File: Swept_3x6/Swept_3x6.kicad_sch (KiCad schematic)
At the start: 94 parts, among them SW10 SW_Push, SW10_r1 SW_Push, SW11 SW_Push, SW11_r1 SW_Push, SW12 SW_Push, SW12_r1 SW_Push, SW13 SW_Push, SW13_r1 SW_Push, SW14 SW_Push, SW14_r1 SW_Push, SW15 SW_Push, SW15_r1 SW_Push, SW16 SW_Push, SW16_r1 SW_Push, SW17 SW_Push, SW17_r1 SW_Push, SW18 SW_Push, SW18_r1 SW_Push, SW19 SW_Push, SW19_r1 SW_Push, SW2 SW_Push, SW20 SW_Push, SW20_r1 SW_Push, SW21 SW_Push, SW21_r1 SW_Push, SW22 SW_Push, SW22_r1 SW_Push, SW2_r1 SW_Push, SW3 SW_Push, SW3_r1 SW_Push, SW4 SW_Push, SW4_r1 SW_Push, SW5 SW_Push, SW5_r1 SW_Push, SW6 SW_Push, SW6_r1 SW_Push, SW7 SW_Push, SW7_r1 SW_Push, SW8 SW_Push, SW8_r1 SW_Push, SW9 SW_Push, SW9_r1 SW_Push, U1 ProMicro-kbd, U2 ProMicro-kbd

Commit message: Added support for Kailh hot-swap sockets.
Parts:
- D0, D1, D10, D11, D12, D13, D14, D15, D16, D17, D18, D19, D2, D20, D3, D4, D5, D6, D7, D8, D9, Dr0, Dr1, Dr10, Dr11, Dr12, Dr13, Dr14, Dr15, Dr16, Dr17, Dr18, Dr19, Dr2, Dr20, Dr3, Dr4, Dr5, Dr6, Dr7, Dr8, Dr9: LCSC (none) -> C2099
- SW10, SW10_r1, SW11, SW11_r1, SW12, SW12_r1, SW13, SW13_r1, SW14, SW14_r1, SW15, SW15_r1, SW16, SW16_r1, SW17, SW17_r1, SW18, SW18_r1, SW19, SW19_r1, SW2, SW20, SW20_r1, SW21, SW21_r1, SW22, SW22_r1, SW2_r1, SW3, SW3_r1, SW4, SW4_r1, SW5, SW5_r1, SW6, SW6_r1, SW7, SW7_r1, SW8, SW8_r1, SW9, SW9_r1: footprint aym1607:choc-v1-with-millmax -> keyswitches:Kailh_socket_PG1350_optional

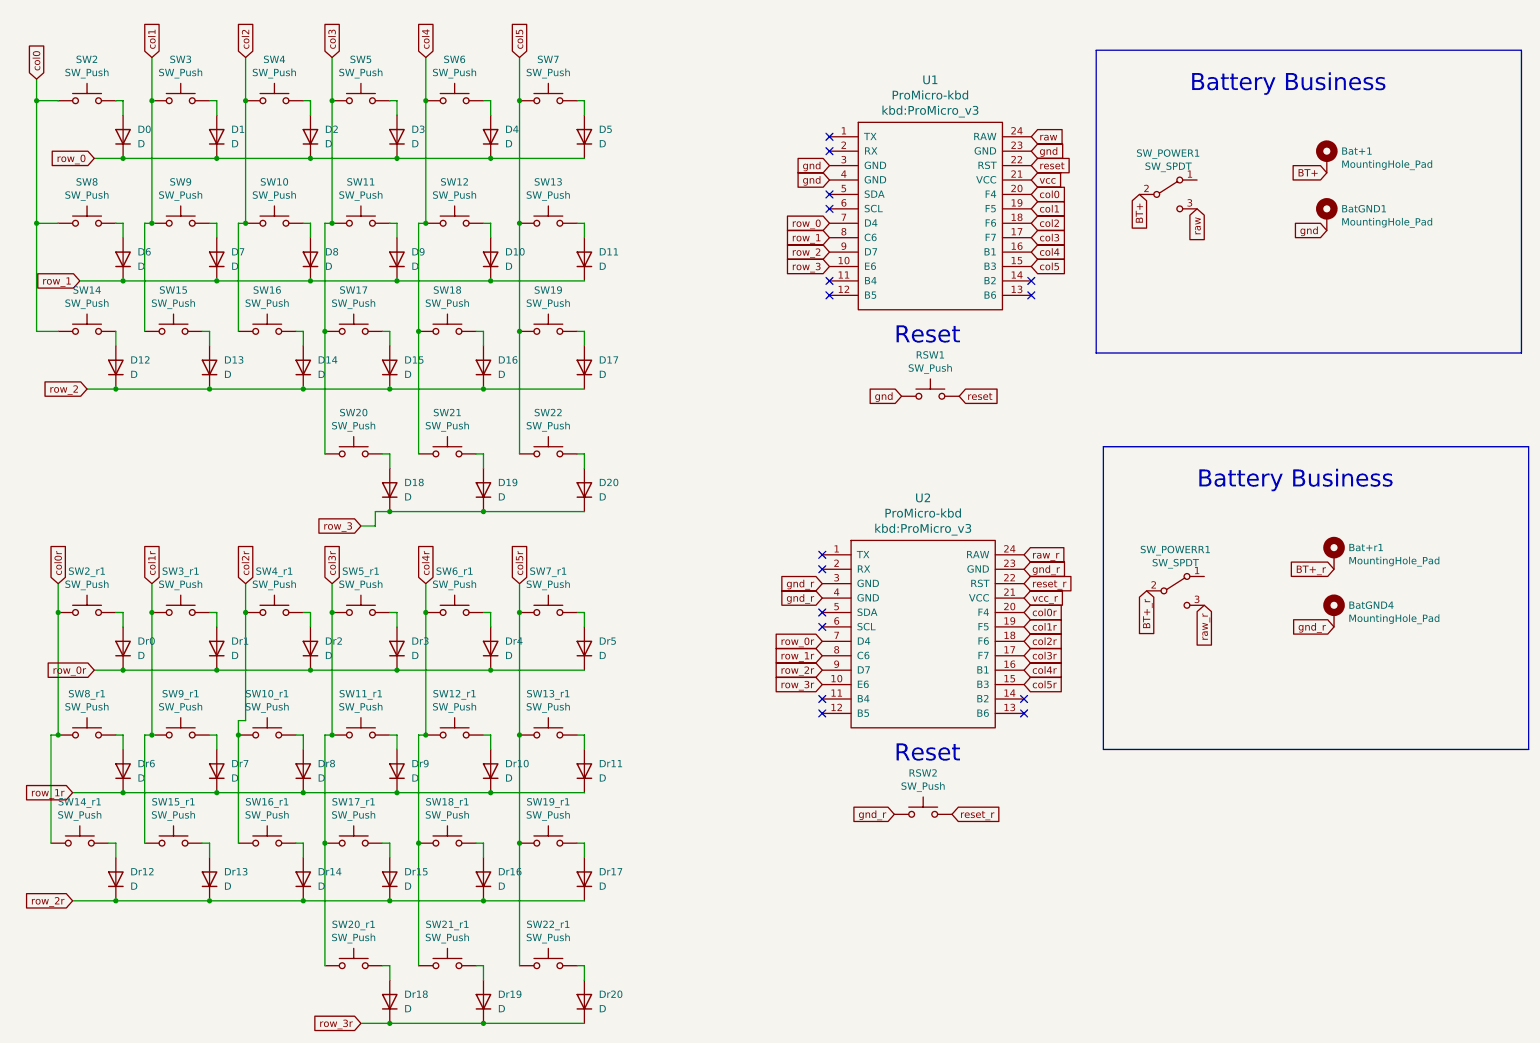
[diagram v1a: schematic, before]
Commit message: Added nice!view suppor for 3x6
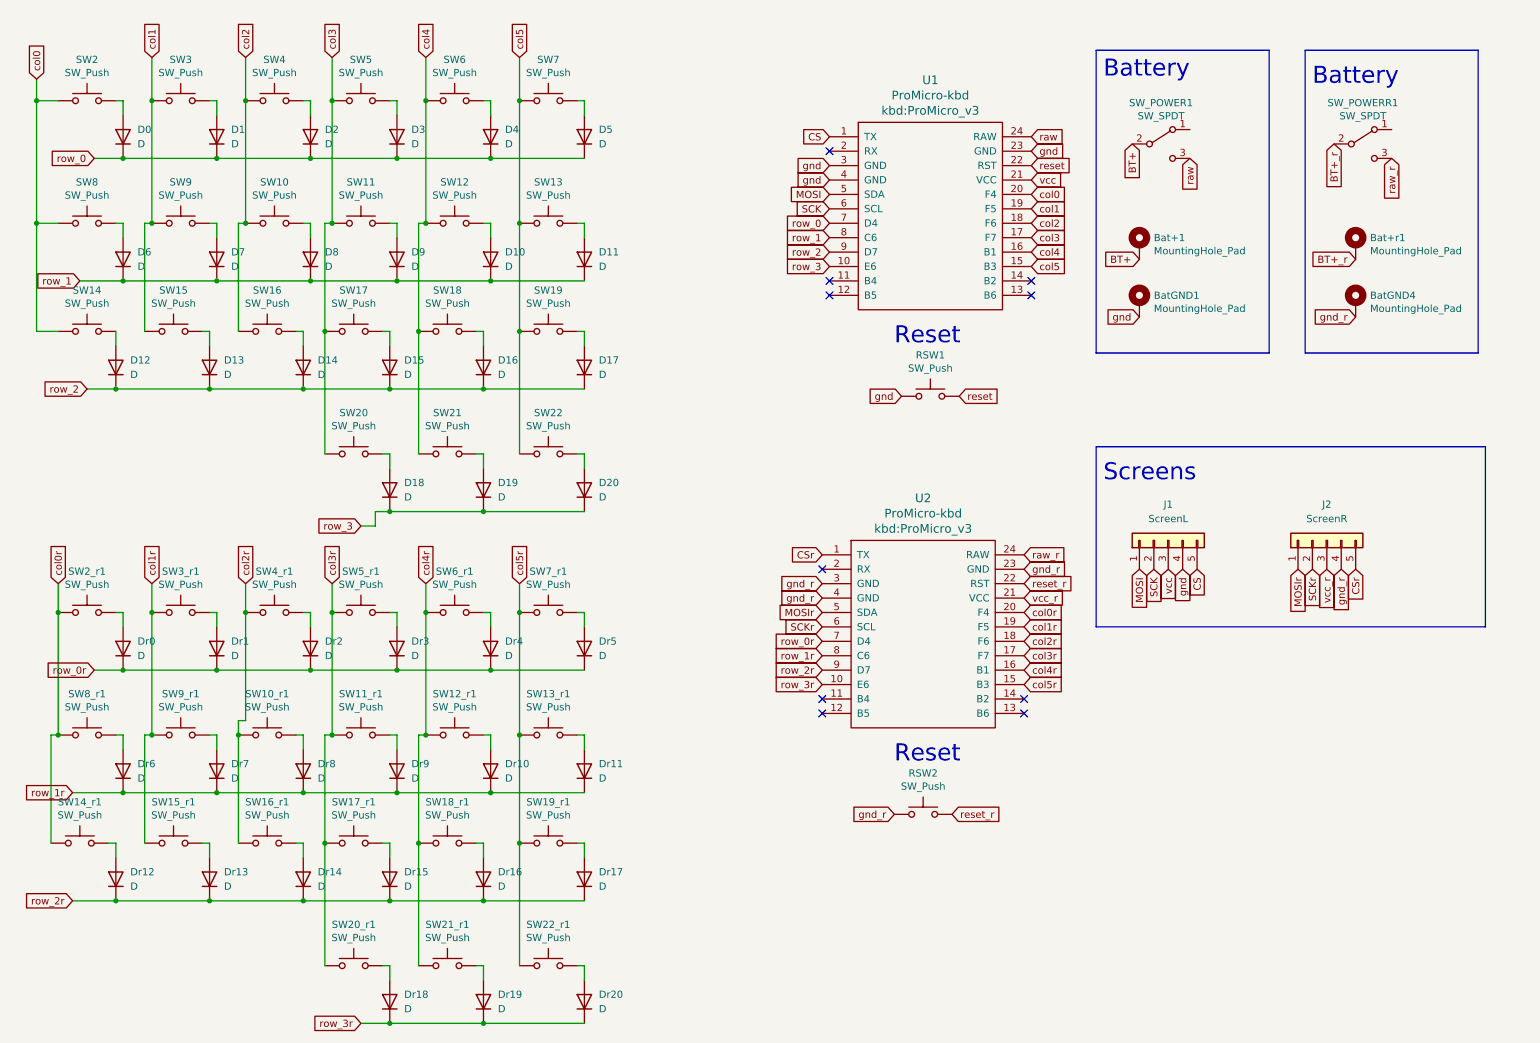
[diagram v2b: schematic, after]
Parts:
- added J1: ScreenL, symbol Connector_Generic:Conn_01x05
- added J2: ScreenR, symbol Connector_Generic:Conn_01x05
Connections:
- net gnd: now also J1.4 (Pin_4)
- net gnd_r: now also J2.4 (Pin_4)
- net vcc: now also J1.3 (Pin_3)
- net vcc_r: now also J2.3 (Pin_3)
- net CS: now reaches U1.1 (TX)
- net CS: now also J1.5 (Pin_5)
- net MOSI: now reaches U1.5 (SDA)
- net MOSI: now also J1.1 (Pin_1)
- net SCK: now reaches U1.6 (SCL)
- net SCK: now also J1.2 (Pin_2)
- net CSr: now reaches U2.1 (TX)
- net CSr: now also J2.5 (Pin_5)
- net MOSIr: now reaches U2.5 (SDA)
- net MOSIr: now also J2.1 (Pin_1)
- net SCKr: now reaches U2.6 (SCL)
- net SCKr: now also J2.2 (Pin_2)
- no-connect marks 16 -> 10
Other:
- note added: "Battery"
- note added: "Screens"
- note removed: "Battery Business"
- moved on the sheet: Bat+1, Bat+r1, BatGND1, BatGND4, SW_POWER1, SW_POWERR1

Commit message: Added nice!view support for 3x5
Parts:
- J1, J2: footprint (none) -> Connector_PinHeader_2.54mm:PinHeader_1x05_P2.54mm_Vertical
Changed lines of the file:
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@@
     (property "Reference" "J1" (id 0) (at 218.44 100.33 90))
     (property "Value" "ScreenL" (id 1) (at 218.44 102.87 90))
-    (property "Footprint" "" (id 2) (at 218.44 106.68 0)
+    (property "Footprint" "Connector_PinHeader_2.54mm:PinHeader_1x05_P2.54mm_Vertical" (id 2) (at 218.44 106.68 0)
       (effects (font (size 1.27 1.27)) hide)
     )
@@
     (property "Reference" "J2" (id 0) (at 246.38 100.33 90))
     (property "Value" "ScreenR" (id 1) (at 246.38 102.87 90))
-    (property "Footprint" "" (id 2) (at 246.38 106.68 0)
+    (property "Footprint" "Connector_PinHeader_2.54mm:PinHeader_1x05_P2.54mm_Vertical" (id 2) (at 246.38 106.68 0)
       (effects (font (size 1.27 1.27)) hide)
     )
@@
     )
     (path "/117e1457-dcde-46f8-812a-e795046b85d7"
-      (reference "J1") (unit 1) (value "ScreenL") (footprint "")
+      (reference "J1") (unit 1) (value "ScreenL") (footprint "Connector_PinHeader_2.54mm:PinHeader_1x05_P2.54mm_Vertical")
     )
     (path "/c13aa899-8898-4a96-864c-f5e8809eb140"
-      (reference "J2") (unit 1) (value "ScreenR") (footprint "")
+      (reference "J2") (unit 1) (value "ScreenR") (footprint "Connector_PinHeader_2.54mm:PinHeader_1x05_P2.54mm_Vertical")
     )
     (path "/00000000-0000-0000-0000-0000604ea4f3"
